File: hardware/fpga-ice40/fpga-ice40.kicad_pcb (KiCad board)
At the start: 4 copper layers, 53.4 x 49.2 mm, 99 parts, among them J1 Conn_01x03, J2 MicroSD_Molex_1040310811, J3 FTSH-105-01-L-DV-K, J4 FTSH-105-01-L-DV-K, J5 USB_B_Micro, J6 Conn_02x20_Odd_Even, Q1 2N7002H-7, U1 iCE40HX4K-TQ144, U10 MC74HC1G08DTT1G, U11 USBLC6-2SC6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

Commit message: More trace glossing
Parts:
- moved C41 0.36 mm to (153.0, 84.5)
- moved C10 0.15 mm to (186.7, 103.0)
- moved C7 0.15 mm to (186.7, 104.5)
- moved C36 0.10 mm to (150.3, 100.5), turned to 180 degrees
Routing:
- net GND: track 184.1 -> 190.6 mm
- net N64_AD0: track 26.7 -> 26.1 mm
- net DRAM_DQ4: track 23.0 -> 22.4 mm

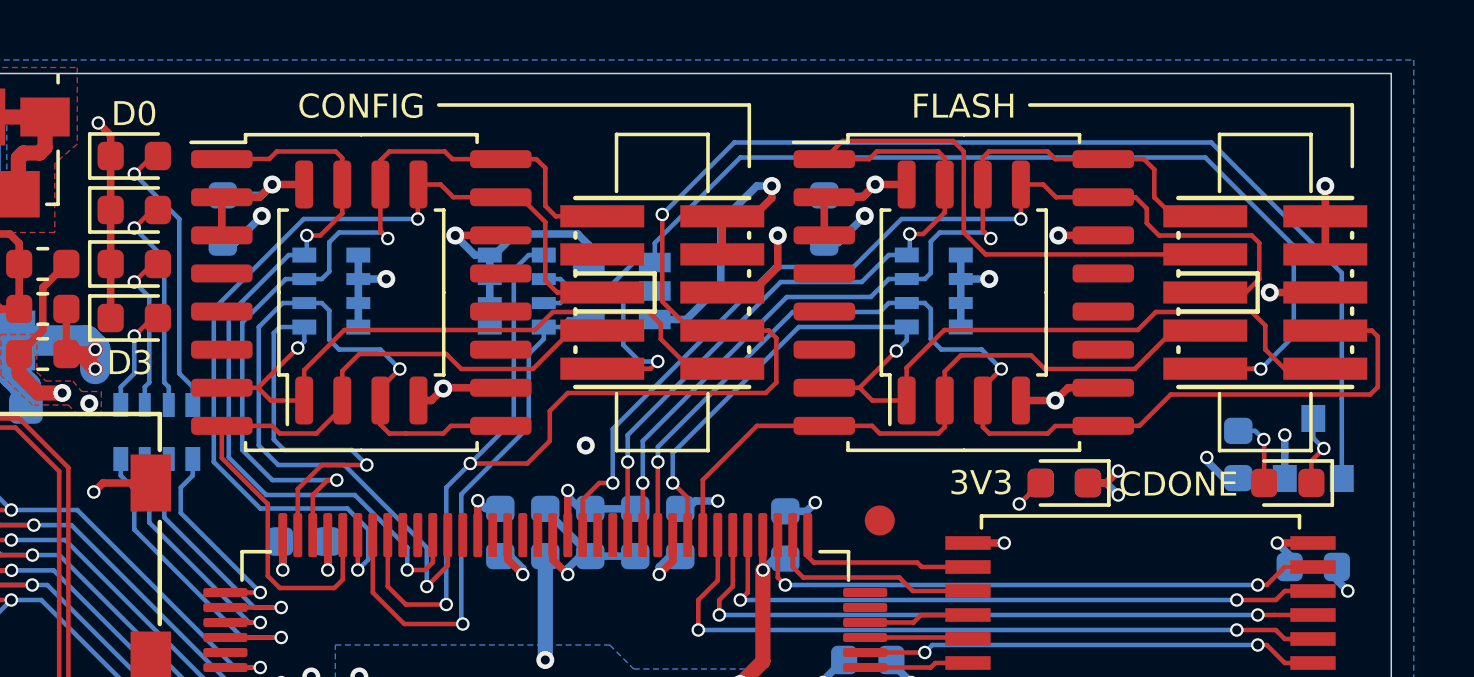
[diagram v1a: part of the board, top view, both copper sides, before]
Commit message: Standardize programming header pinouts for QSPI breakouts
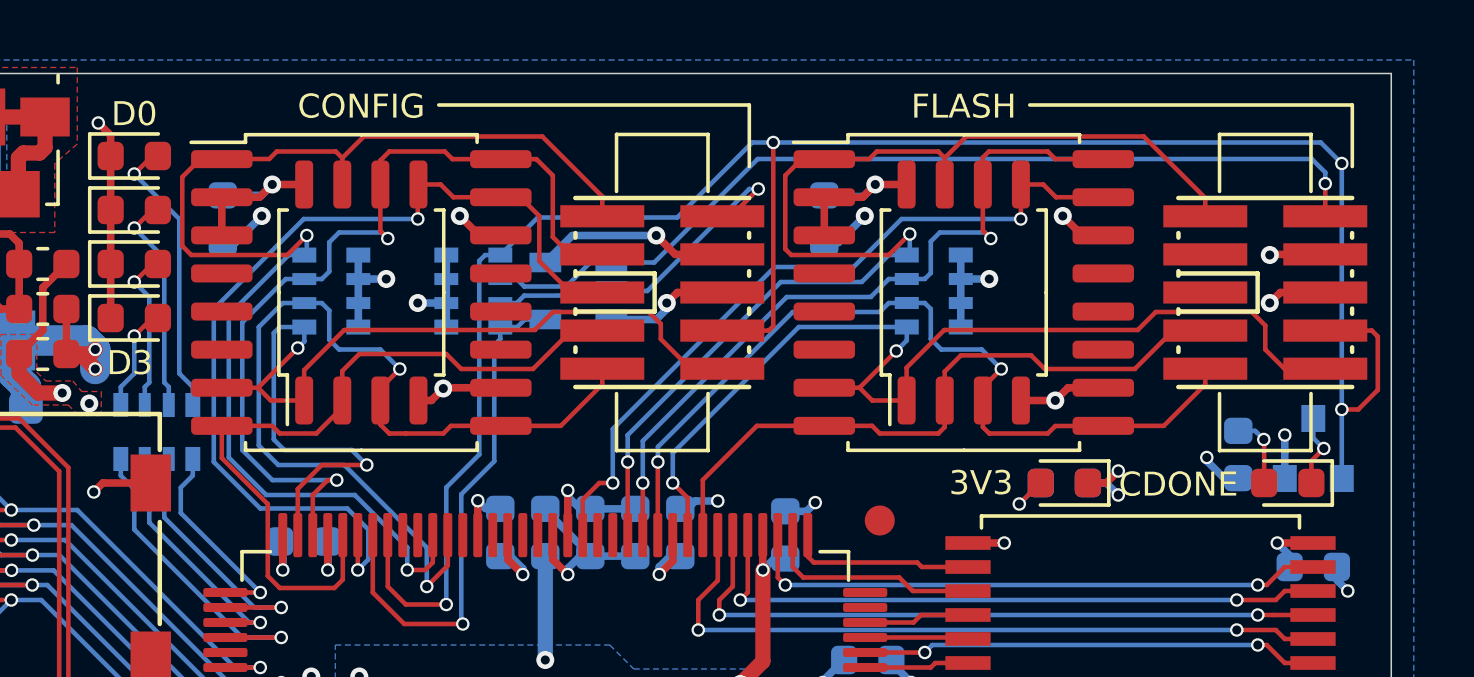
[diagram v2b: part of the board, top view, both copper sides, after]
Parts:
- moved RN10 1.45 mm to (158.7, 76.2)
- moved U10 1.45 mm to (162.2, 76.2)
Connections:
- J3 pad 1: CONFIG_SCK -> CONFIG_IO3
- J3 pad 2: GND -> CONFIG_CRESETn
- J3 pad 3: Net-(J3-Pad3) -> CONFIG_SCK
- J3 pad 4: GND -> P3V3
- J3 pad 6: P3V3 -> GND
- J3 pad 9: CONFIG_CRESETn -> CONFIG_IO2
- J4 pad 1: FLASH_SCK -> FLASH_IO3
- J4 pad 2: GND -> FLASH_CRESETn
- J4 pad 3: FLASH_IO3 -> FLASH_SCK
- J4 pad 4: GND -> P3V3
- J4 pad 6: P3V3 -> GND
- J4 pad 8: FLASH_IO2 -> FPGA_CDONE
- J4 pad 9: FLASH_CRESETn -> FLASH_IO2
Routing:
- net CONFIG_IO3: track 26.2 -> 42.6 mm
- net FLASH_MOSI|IO0: track 34.1 -> 24.8 mm
- net FLASH_IO2: track 37.5 -> 28.8 mm
- net GND: track 190.6 -> 183.9 mm, vias 65 -> 64
- net FLASH_SCK: track 30.1 -> 25.3 mm
- net CONFIG_IO2: track 27.9 -> 32.4 mm
- net FLASH_CRESETn: track 34.6 -> 31.0 mm
- net CONFIG_CRESETn: track 8.89 -> 11.8 mm
- net CONFIG_MOSI|IO0: track 33.8 -> 32.1 mm
- net P3V3: track 110.8 -> 109.7 mm, vias 39 -> 40
- net CONFIG_SCK: track 30.4 -> 29.8 mm
- net FPGA_CRESETn: track 18.2 -> 17.6 mm
- net FPGA_CDONE: track 70.1 -> 70.0 mm, vias 3 -> 4

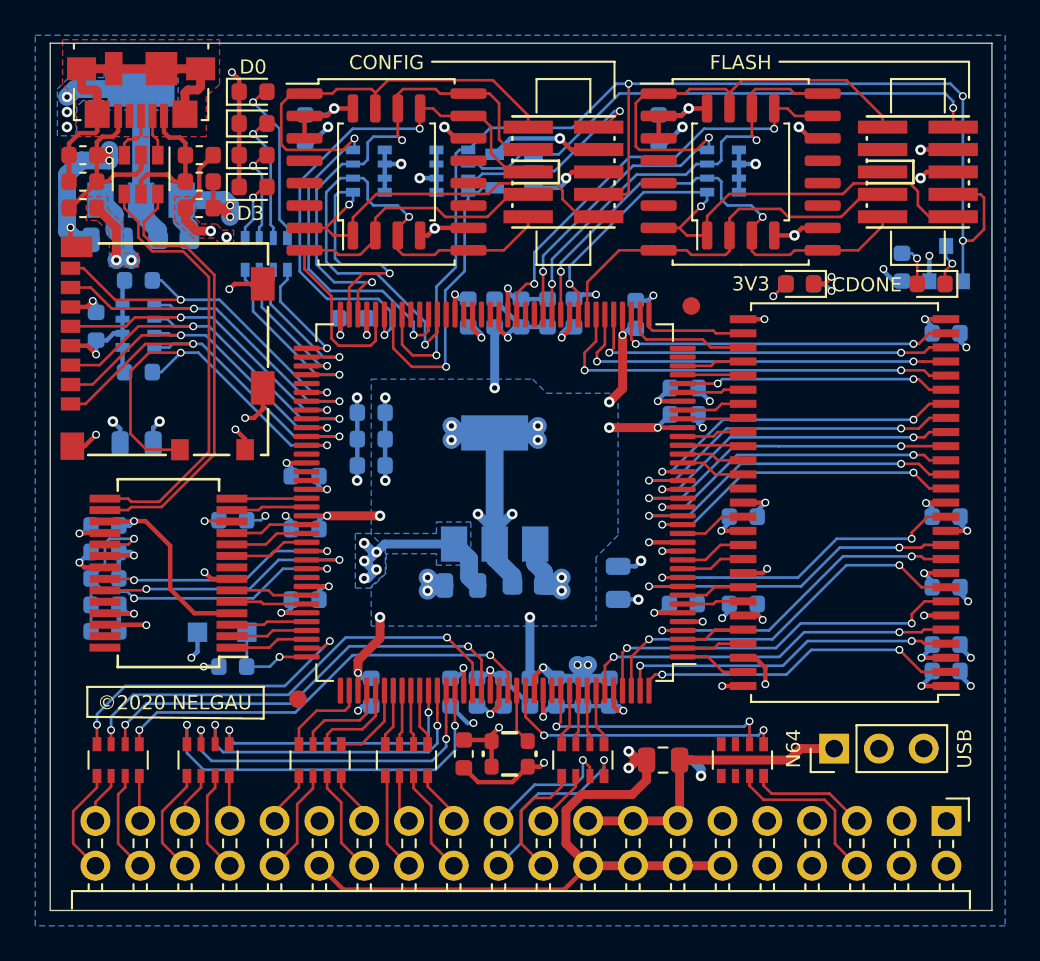
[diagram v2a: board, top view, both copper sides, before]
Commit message: Fix a few via/silkscreen collisions
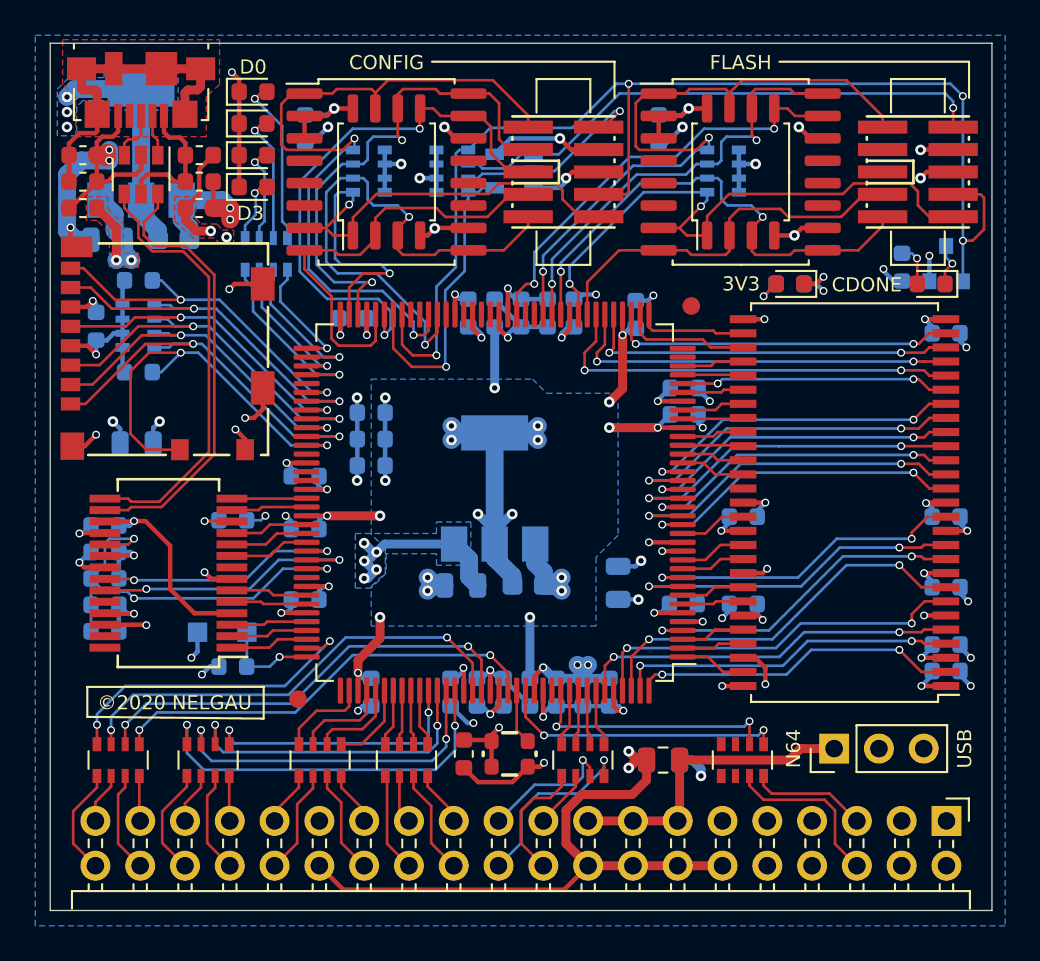
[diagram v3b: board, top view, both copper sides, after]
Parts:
- moved D7 0.55 mm to (177.8, 82.6)
- moved R13 0.55 mm to (177.8, 82.6)
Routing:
- net GND: track 183.9 -> 182.7 mm

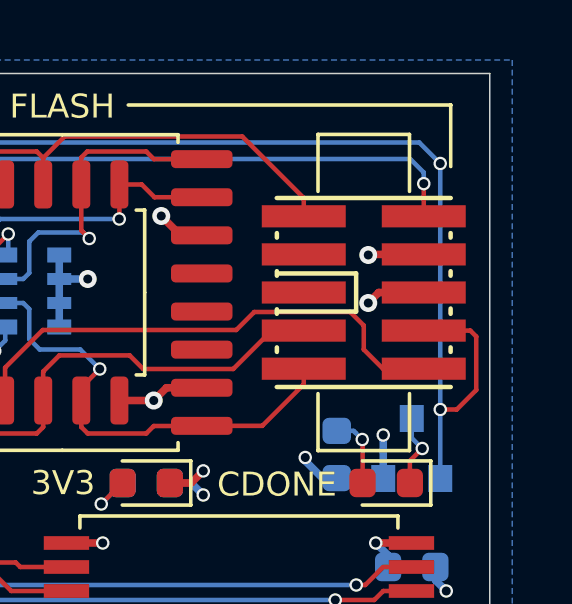
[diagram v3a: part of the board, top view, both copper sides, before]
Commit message: Minor routing gloss for FPGA_CDONE signal
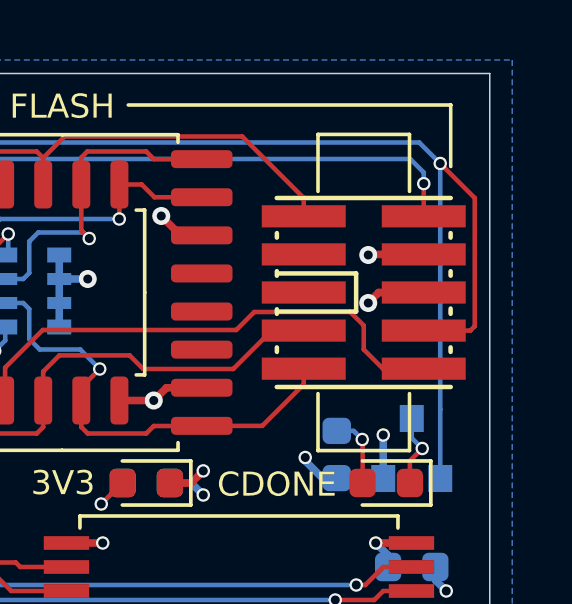
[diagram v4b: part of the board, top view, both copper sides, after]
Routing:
- net FPGA_CDONE: track 70.0 -> 72.5 mm, vias 4 -> 3
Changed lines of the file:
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@@
     (thickness 1.2)
     (drawings 23)
-    (tracks 1804)
+    (tracks 1802)
     (zones 0)
     (modules 99)
@@
   )
   (setup
-    (last_trace_width 1.016)
+    (last_trace_width 0.1524)
     (user_trace_width 0.1524)
     (user_trace_width 0.254)
@@
   (segment (start 145.4125 104.3) (end 144.9 104.3) (width 0.254) (layer B.Cu) (net 12))
   (segment (start 144.9 104.3) (end 144.45 104.75) (width 0.254) (layer B.Cu) (net 12))
-  (via (at 187.6 80.15) (size 0.45) (drill 0.3) (layers F.Cu B.Cu) (net 19))
-  (segment (start 188.15 80.15) (end 187.6 80.15) (width 0.1524) (layer F.Cu) (net 19))
-  (segment (start 188.8 77.7176) (end 188.8 79.5) (width 0.1524) (layer F.Cu) (net 19))
-  (segment (start 188.8 79.5) (end 188.15 80.15) (width 0.1524) (layer F.Cu) (net 19))
-  (segment (start 188.6024 77.52) (end 188.8 77.7176) (width 0.1524) (layer F.Cu) (net 19))
-  (segment (start 187.05 77.52) (end 188.6024 77.52) (width 0.1524) (layer F.Cu) (net 19))
   (segment (start 158.85 81.65) (end 157.75 82.75) (width 0.1524) (layer B.Cu) (net 19))
   (segment (start 157.75 82.75) (end 157.75 86.649998) (width 0.1524) (layer B.Cu) (net 19))
@@
   (segment (start 187.6 80.15) (end 187.6 71.95) (width 0.1524) (layer B.Cu) (net 19))
   (via (at 187.6 71.95) (size 0.45) (drill 0.3) (layers F.Cu B.Cu) (net 19))
+  (segment (start 188.6024 77.52) (end 187.05 77.52) (width 0.1524) (layer F.Cu) (net 19))
+  (segment (start 188.75 77.3724) (end 188.6024 77.52) (width 0.1524) (layer F.Cu) (net 19))
+  (segment (start 188.75 73.1) (end 188.75 77.3724) (width 0.1524) (layer F.Cu) (net 19))
+  (segment (start 187.6 71.95) (end 188.75 73.1) (width 0.1524) (layer F.Cu) (net 19))
   (segment (start 158.25 87.25) (end 158.3 87.3) (width 0.1524) (layer B.Cu) (net 20))
   (segment (start 158.25 82.975) (end 158.25 87.25) (width 0.1524) (layer B.Cu) (net 20))
